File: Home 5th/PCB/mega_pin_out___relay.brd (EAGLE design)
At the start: 100 x 85 mm, 43 parts, among them K1 G5Q-1-EU DC12, K2 G5Q-1-EU DC12, K3 G5Q-1-EU DC12, K4 G5Q-1-EU DC12

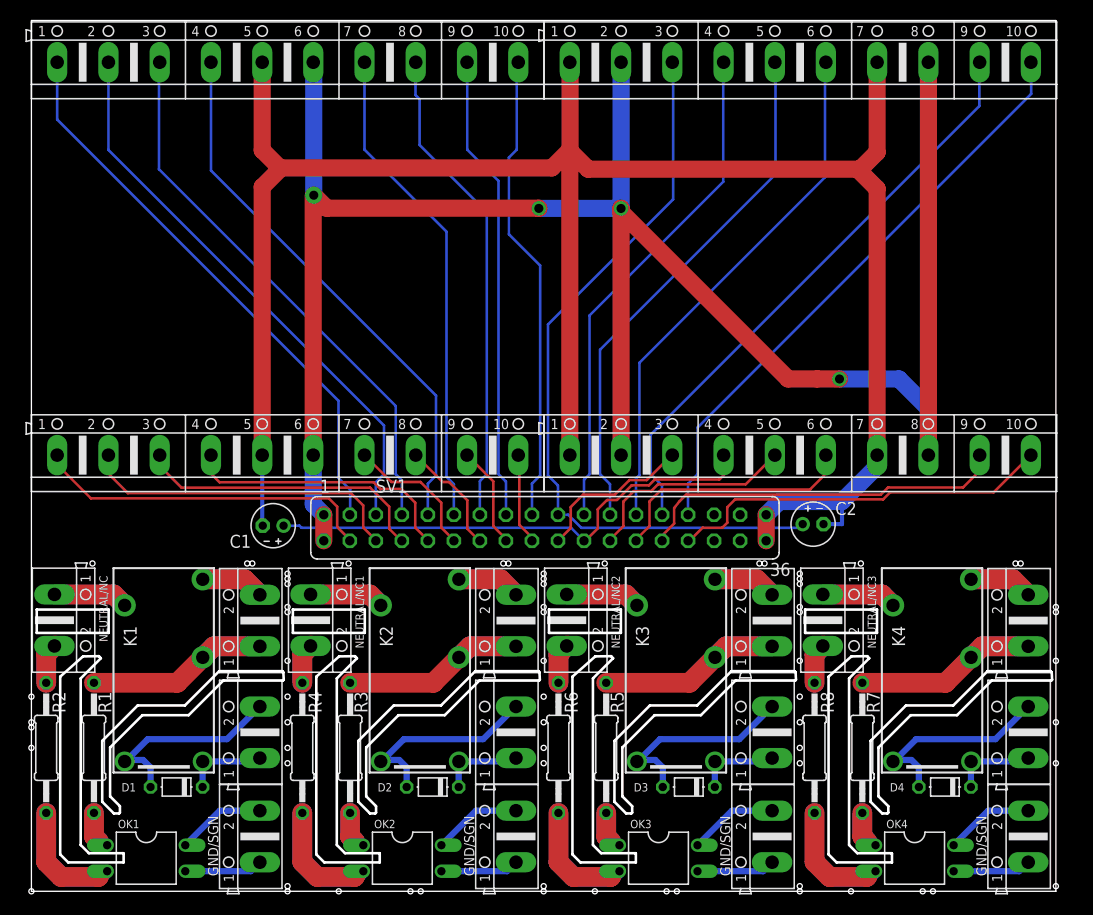
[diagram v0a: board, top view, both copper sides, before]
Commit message: Adding and removing some Drill holes
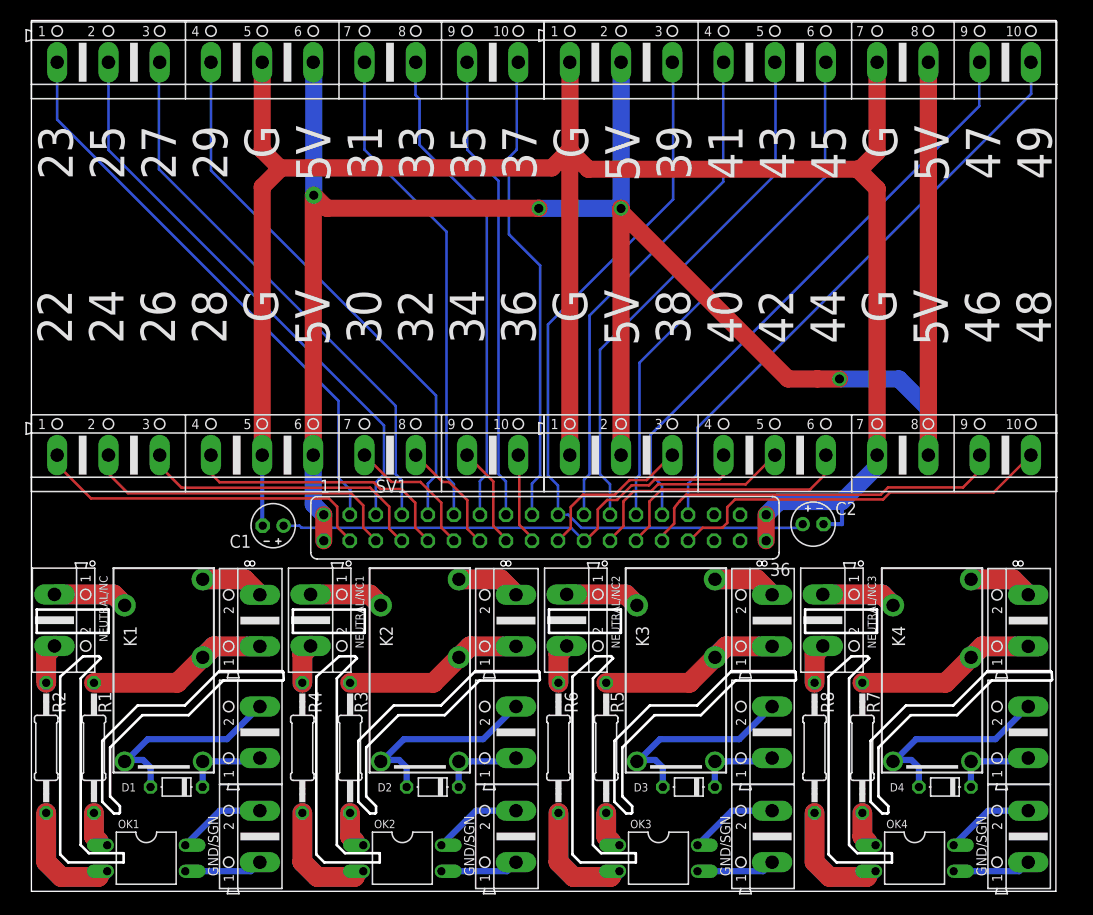
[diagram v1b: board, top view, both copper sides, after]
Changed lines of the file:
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@@
 <?xml version="1.0" encoding="utf-8"?>
 <!DOCTYPE eagle SYSTEM "eagle.dtd">
-<eagle version="7.7.0">
+<eagle version="7.3.0">
 <drawing>
 <settings>
@@
 <wire x1="100" y1="85" x2="0" y2="85" width="0" layer="20"/>
 <wire x1="0" y1="85" x2="0" y2="0" width="0" layer="20"/>
-<dimension x1="37.8968" y1="77.3176" x2="0.6096" y2="46.5328" x3="6.7056" y3="61.9252" textsize="1.778" layer="1" dtype="vertical"/>
-<dimension x1="0" y1="85" x2="28.5496" y2="32.004" x3="-1.6256" y3="58.502" textsize="1.778" layer="1" dtype="vertical"/>
-<dimension x1="0" y1="0" x2="0" y2="32.004" x3="-3.7592" y3="16.002" textsize="1.778" layer="1"/>
-<text x="0.60198125" y="58.7248" size="3.3528" layer="26" rot="R270">22
+<text x="0.60198125" y="58.7248" size="3.3528" layer="25" rot="R270">22
 24
 26
@@
 46
 48</text>
-<text x="0.6858" y="74.744578125" size="3.3528" layer="26" rot="R270">23
+<text x="0.6858" y="74.744578125" size="3.3528" layer="25" rot="R270">23
 25
 27
@@
 <text x="61.866778125" y="68.684140625" size="1.9558" layer="26" rot="R270">Light</text>
 <text x="17.233" y="7.3866" size="1" layer="25" rot="R270">GND/SGN</text>
-<hole x="25" y="27.75" drill="0.5"/>
-<hole x="25" y="27.25" drill="0.5"/>
 <hole x="21.06" y="32" drill="0.5"/>
 <hole x="21.56" y="32" drill="0.5"/>
@@
 <wire x1="24.63" y1="20.65" x2="24.59" y2="21.38" width="0.254" layer="20"/>
 <wire x1="24.59" y1="21.38" x2="24.48" y2="21.49" width="0.254" layer="20"/>
-<hole x="0" y="0" drill="0.5"/>
-<hole x="25" y="0.5" drill="0.5"/>
-<hole x="25" y="12.5" drill="0.5"/>
-<hole x="25" y="16.5" drill="0.5"/>
-<hole x="25" y="22.5" drill="0.5"/>
-<hole x="0" y="19" drill="0.5"/>
-<hole x="0" y="14" drill="0.5"/>
 <text x="42.233" y="7.3866" size="1" layer="25" rot="R270">GND/SGN</text>
-<hole x="50" y="27.75" drill="0.5"/>
-<hole x="50" y="27.25" drill="0.5"/>
 <hole x="46.06" y="32" drill="0.5"/>
 <hole x="46.56" y="32" drill="0.5"/>
@@
 <wire x1="49.63" y1="20.65" x2="49.59" y2="21.38" width="0.254" layer="20"/>
 <wire x1="49.59" y1="21.38" x2="49.48" y2="21.49" width="0.254" layer="20"/>
-<hole x="25" y="31" drill="0.5"/>
-<hole x="25" y="30.5" drill="0.5"/>
-<hole x="25" y="30" drill="0.5"/>
-<hole x="37" y="0" drill="0.5"/>
-<hole x="38" y="0" drill="0.5"/>
-<hole x="30" y="0" drill="0.5"/>
-<hole x="25" y="0" drill="0.5"/>
-<hole x="50" y="0.5" drill="0.5"/>
-<hole x="50" y="12.5" drill="0.5"/>
-<hole x="50" y="16.5" drill="0.5"/>
-<hole x="50" y="22.5" drill="0.5"/>
-<hole x="25" y="19" drill="0.5"/>
-<hole x="25" y="14" drill="0.5"/>
-<hole x="0" y="16.5" drill="0.5"/>
-<hole x="0" y="16" drill="0.5"/>
 <text x="67.233" y="7.3866" size="1" layer="25" rot="R270">GND/SGN</text>
-<hole x="75" y="27.75" drill="0.5"/>
-<hole x="75" y="27.25" drill="0.5"/>
 <hole x="71.06" y="32" drill="0.5"/>
 <hole x="71.56" y="32" drill="0.5"/>
@@
 <wire x1="74.63" y1="20.65" x2="74.59" y2="21.38" width="0.254" layer="20"/>
 <wire x1="74.59" y1="21.38" x2="74.48" y2="21.49" width="0.254" layer="20"/>
-<hole x="50" y="31" drill="0.5"/>
-<hole x="50" y="30.5" drill="0.5"/>
-<hole x="50" y="30" drill="0.5"/>
-<hole x="62" y="0" drill="0.5"/>
-<hole x="63" y="0" drill="0.5"/>
-<hole x="55" y="0" drill="0.5"/>
-<hole x="50" y="0" drill="0.5"/>
-<hole x="75" y="0.5" drill="0.5"/>
-<hole x="75" y="12.5" drill="0.5"/>
-<hole x="75" y="16.5" drill="0.5"/>
-<hole x="75" y="22.5" drill="0.5"/>
-<hole x="50" y="19" drill="0.5"/>
-<hole x="50" y="14" drill="0.5"/>
 <text x="92.233" y="7.3866" size="1" layer="25" rot="R270">GND/SGN</text>
-<hole x="100" y="27.75" drill="0.5"/>
-<hole x="100" y="27.25" drill="0.5"/>
 <hole x="96.06" y="32" drill="0.5"/>
 <hole x="96.56" y="32" drill="0.5"/>
@@
 <wire x1="99.63" y1="20.65" x2="99.59" y2="21.38" width="0.254" layer="20"/>
 <wire x1="99.59" y1="21.38" x2="99.48" y2="21.49" width="0.254" layer="20"/>
-<hole x="75" y="31" drill="0.5"/>
-<hole x="75" y="30.5" drill="0.5"/>
-<hole x="75" y="30" drill="0.5"/>
-<hole x="87" y="0" drill="0.5"/>
-<hole x="88" y="0" drill="0.5"/>
-<hole x="80" y="0" drill="0.5"/>
-<hole x="75" y="0" drill="0.5"/>
-<hole x="100" y="0.5" drill="0.5"/>
-<hole x="100" y="12.5" drill="0.5"/>
-<hole x="100" y="16.5" drill="0.5"/>
-<hole x="100" y="22.5" drill="0.5"/>
-<hole x="75" y="19" drill="0.5"/>
-<hole x="75" y="14" drill="0.5"/>
 </plain>
 <attributes>

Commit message: [SIDES] Customize drill holes for the mega_pin_out
- Customize drill holes for the mega_pin_outtom with the mega_sides to avoid overlapping
- To be continued
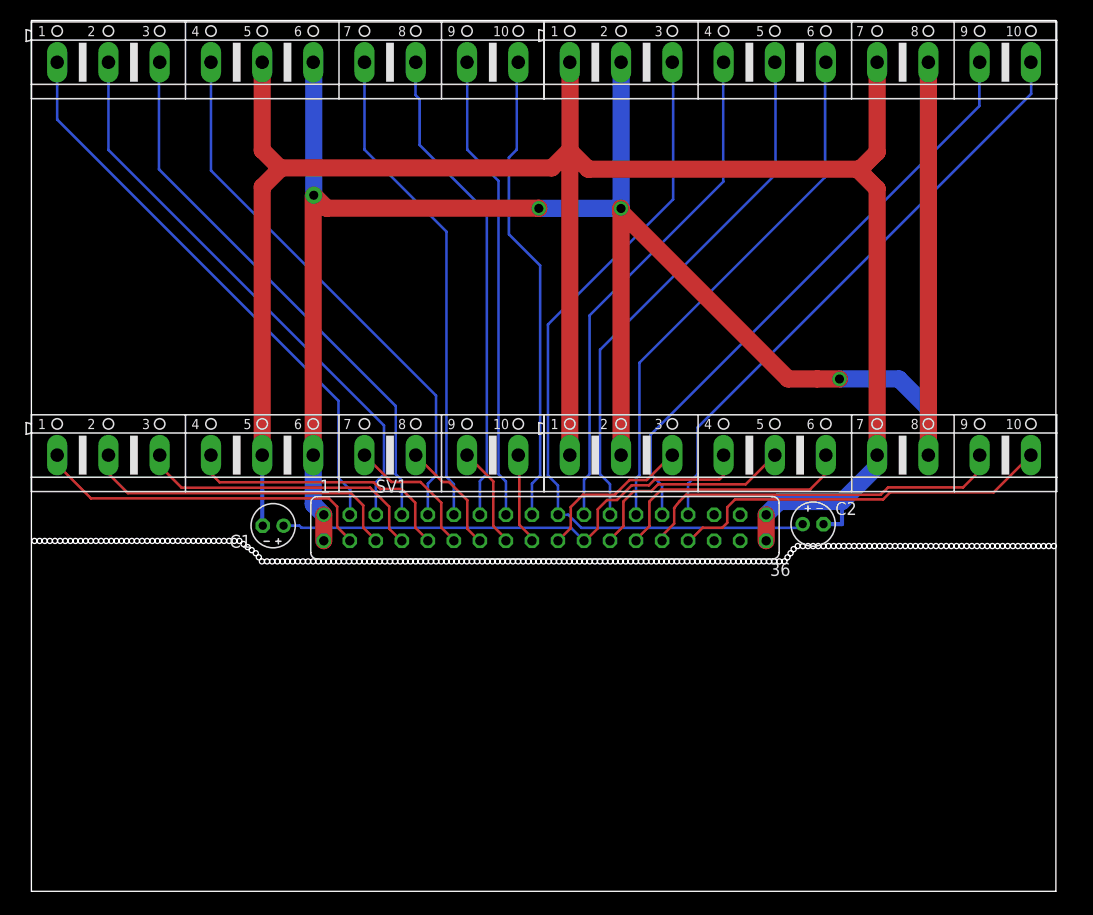
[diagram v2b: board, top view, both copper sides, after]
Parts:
- removed D1, D2, D3, D4: 1N4007, diode:D-5
- removed GND/S, GND/S1, GND/S2, GND/S3, LOAD/NO, LOAD/NO1, LOAD/NO2, LOAD/NO3, NEUTRAL/NC, NEUTRAL/NC1, NEUTRAL/NC2, NEUTRAL/NC3, VEXT/BJT, VEXT/BJT1, VEXT/BJT2, VEXT/BJT3: (no value), con-ptr500-modified:AK500/2
- removed K1, K2, K3, K4: G5Q-1-EU DC12, relay:G5SB
- removed OK1, OK2, OK3, OK4: SFH620A, optocoupler:DIL04
- removed R1, R2, R3, R4, R5, R6, R7, R8: 22k/2W, rcl:0207/12
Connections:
- removed net N$12: OK1.1, R1.2
- removed net N$25: D1.C, K1.1, VEXT/BJT.1
- removed net N$30: D1.A, K1.5, VEXT/BJT.2
- removed net N$31: K1.3, LOAD/NO.2
- removed net N$32: GND/S.2, OK1.4
- removed net N$33: GND/S.1, OK1.3
- removed net N$34: K2.2, LOAD/NO1.1, R3.1
- removed net N$35: NEUTRAL/NC1.2, R4.1
- removed net N$36: K2.4, NEUTRAL/NC1.1
- removed net N$37: OK2.2, R4.2
- removed net N$38: OK2.1, R3.2
- removed net N$39: D2.C, K2.1, VEXT/BJT1.1
- removed net N$40: D2.A, K2.5, VEXT/BJT1.2
- removed net N$41: K2.3, LOAD/NO1.2
- removed net N$42: GND/S1.2, OK2.4
- removed net N$43: GND/S1.1, OK2.3
- removed net N$44: K3.2, LOAD/NO2.1, R5.1
- removed net N$45: NEUTRAL/NC2.2, R6.1
- removed net N$46: K3.4, NEUTRAL/NC2.1
- removed net N$47: OK3.2, R6.2
- removed net N$48: OK3.1, R5.2
- removed net N$49: D3.C, K3.1, VEXT/BJT2.1
- removed net N$5: K1.2, LOAD/NO.1, R1.1
- removed net N$50: D3.A, K3.5, VEXT/BJT2.2
- removed net N$51: K3.3, LOAD/NO2.2
- removed net N$52: GND/S2.2, OK3.4
- removed net N$53: GND/S2.1, OK3.3
- removed net N$54: K4.2, LOAD/NO3.1, R7.1
- removed net N$55: NEUTRAL/NC3.2, R8.1
- removed net N$56: K4.4, NEUTRAL/NC3.1
- removed net N$57: OK4.2, R8.2
- removed net N$58: OK4.1, R7.2
- removed net N$59: D4.C, K4.1, VEXT/BJT3.1
- removed net N$6: NEUTRAL/NC.2, R2.1
- removed net N$60: D4.A, K4.5, VEXT/BJT3.2
- removed net N$61: K4.3, LOAD/NO3.2
- removed net N$62: GND/S3.2, OK4.4
- removed net N$63: GND/S3.1, OK4.3
- removed net N$7: K1.4, NEUTRAL/NC.1
- removed net N$8: OK1.2, R2.2
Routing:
- net N$5: track 23.5 -> 0.00 mm
- net N$44: track 23.5 -> 0.00 mm
- net N$34: track 23.5 -> 0.00 mm
- net N$54: track 23.5 -> 0.00 mm
- net N$57: track 23.1 -> 0.00 mm
- net N$37: track 23.1 -> 0.00 mm
- net N$8: track 23.1 -> 0.00 mm
- net N$47: track 23.1 -> 0.00 mm
- net N$50: track 19.8 -> 0.00 mm
- net N$40: track 19.8 -> 0.00 mm
- net N$30: track 19.8 -> 0.00 mm
- net N$60: track 19.8 -> 0.00 mm
- net N$56: track 14.5 -> 0.00 mm
- net N$7: track 14.5 -> 0.00 mm
- net N$36: track 14.5 -> 0.00 mm
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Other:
- outline, holes or cut-outs redrawn
- board text removed: "GND/SGN"

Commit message: [V0.1] Mega with Relay
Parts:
- added D1, D2, D3, D4: 1N4007, diode:D-5
- added GND/S1, GND/S2, GND/S3, GND/S4, LOAD/NO1, LOAD/NO2, LOAD/NO3, LOAD/NO4, NEUTRAL/NC, NEUTRAL/NC1, NEUTRAL/NC2, NEUTRAL/NC4, VEXT/BJT, VEXT/BJT2, VEXT/BJT3, VEXT/BJT4: (no value), con-ptr500-modified:AK500/2
- added K1, K2, K3, K4: G5Q-1-EU DC12, relay:G5SB
- added OK1, OK2, OK3, OK4: SFH620A, optocoupler:DIL04
- added R1, R2, R3, R4, R5, R6, R7, R8: 22k/2W, rcl:0207/12
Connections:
- new net N$12: D3.C, K3.1, VEXT/BJT2.1
- new net N$25: OK3.1, R5.2
- new net N$30: D3.A, K3.5, VEXT/BJT2.2
- new net N$31: K3.3, LOAD/NO2.2
- new net N$32: GND/S2.2, OK3.4
- new net N$33: GND/S2.1, OK3.3
- new net N$34: K1.2, LOAD/NO1.1, R1.1
- new net N$35: NEUTRAL/NC1.2, R2.1
- new net N$36: K1.4, NEUTRAL/NC1.1
- new net N$37: OK1.2, R2.2
- new net N$38: OK1.1, R1.2
- new net N$39: D1.C, K1.1, VEXT/BJT.1
- new net N$40: D1.A, K1.5, VEXT/BJT.2
- new net N$41: K1.3, LOAD/NO1.2
- new net N$42: GND/S1.2, OK1.4
- new net N$43: GND/S1.1, OK1.3
- new net N$44: K2.2, LOAD/NO3.1, R3.1
- new net N$45: NEUTRAL/NC.2, R4.1
- new net N$46: K2.4, NEUTRAL/NC.1
- new net N$47: OK2.2, R4.2
- new net N$48: OK2.1, R3.2
- new net N$49: D2.C, K2.1, VEXT/BJT3.1
- new net N$5: K3.2, LOAD/NO2.1, R5.1
- new net N$50: D2.A, K2.5, VEXT/BJT3.2
- new net N$51: K2.3, LOAD/NO3.2
- new net N$52: GND/S3.2, OK2.4
- new net N$53: GND/S3.1, OK2.3
- new net N$54: K4.2, LOAD/NO4.1, R7.1
- new net N$55: NEUTRAL/NC4.2, R8.1
- new net N$56: K4.4, NEUTRAL/NC4.1
- new net N$57: OK4.2, R8.2
- new net N$58: OK4.1, R7.2
- new net N$59: D4.C, K4.1, VEXT/BJT4.1
- new net N$6: NEUTRAL/NC2.2, R6.1
- new net N$60: D4.A, K4.5, VEXT/BJT4.2
- new net N$61: K4.3, LOAD/NO4.2
- new net N$62: GND/S4.2, OK4.4
- new net N$63: GND/S4.1, OK4.3
- new net N$7: K3.4, NEUTRAL/NC2.1
- new net N$8: OK3.2, R6.2
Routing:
- net N$54: track 0.00 -> 23.5 mm
- net N$44: track 0.00 -> 23.5 mm
- net N$5: track 0.00 -> 23.5 mm
- net N$34: track 0.00 -> 23.5 mm
- net N$57: track 0.00 -> 23.1 mm
- net N$47: track 0.00 -> 23.1 mm
- net N$8: track 0.00 -> 23.1 mm
- net N$37: track 0.00 -> 23.1 mm
- net N$60: track 0.00 -> 19.8 mm
- net N$40: track 0.00 -> 19.8 mm
- net N$30: track 0.00 -> 19.8 mm
- net N$50: track 0.00 -> 19.8 mm
- net N$46: track 0.00 -> 14.5 mm
- net N$56: track 0.00 -> 14.5 mm
- net N$7: track 0.00 -> 14.5 mm
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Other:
- outline, holes or cut-outs redrawn
- board text added: "D1"
- board text added: "GND/SGN"
- board text added: "K1"
- board text added: "LOAD/NO"
- board text added: "NEUTRAL/NC"
- board text added: "OK1"
- board text added: "R1"
- board text added: "R2"
